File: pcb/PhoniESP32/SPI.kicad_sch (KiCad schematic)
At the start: 6 parts, among them J4 Conn_01x08_Pin

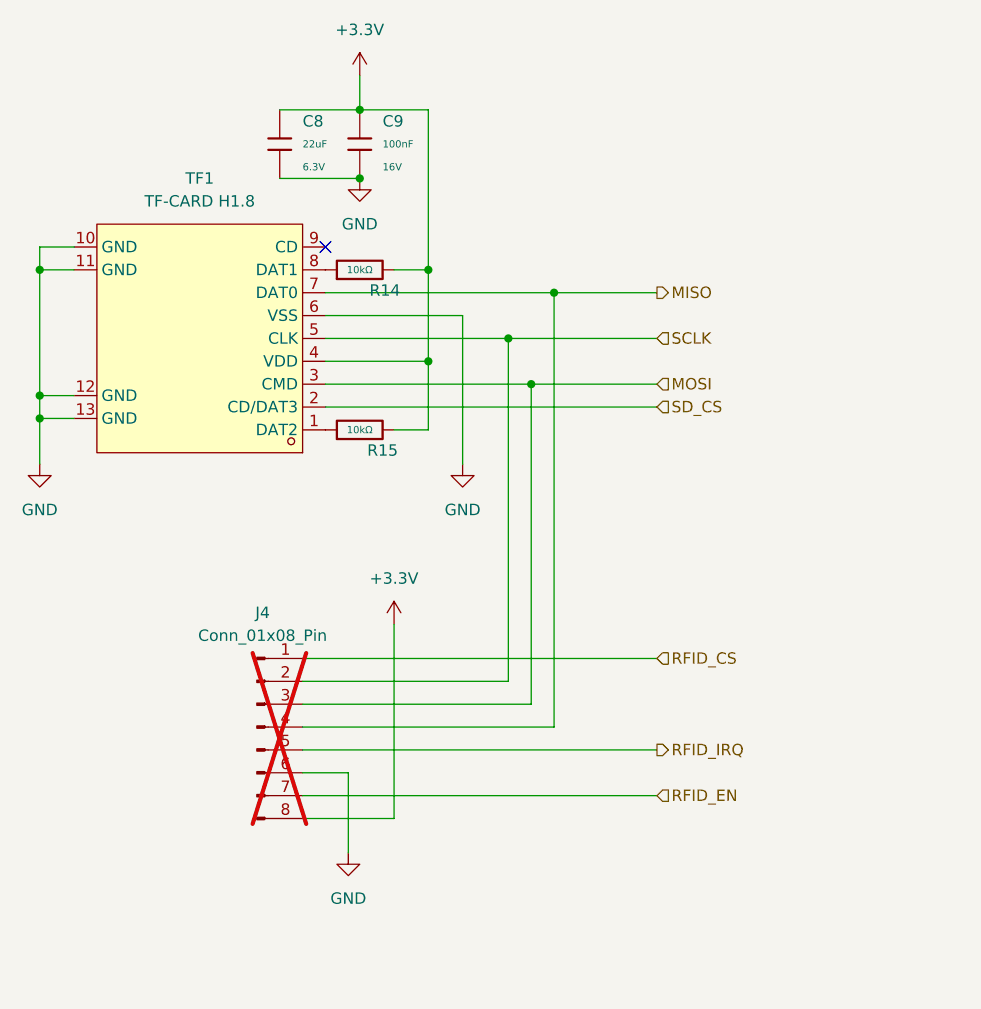
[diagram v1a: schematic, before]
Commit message: feat(pcb): version for hand soldering
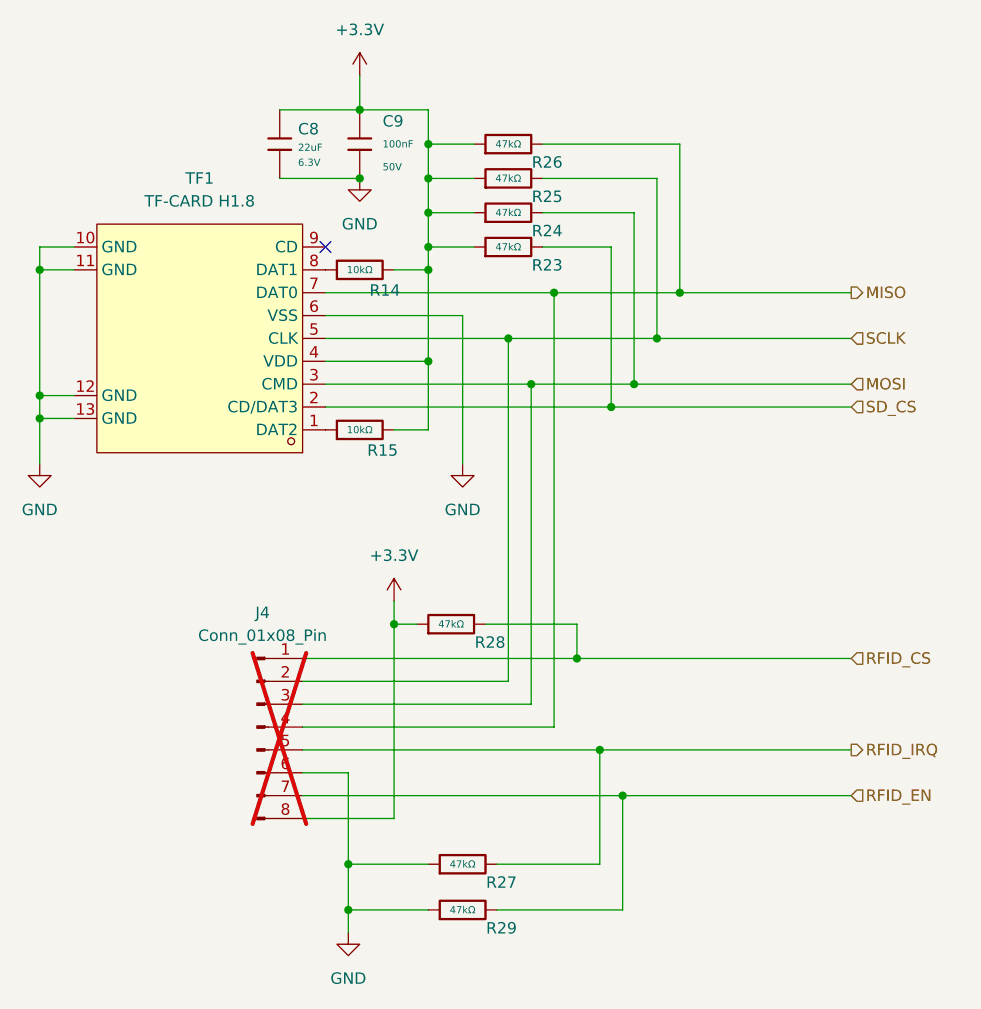
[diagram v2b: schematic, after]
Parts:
- added R23, R24, R25, R26, R27, R28, R29: 47kΩ, PCM_JLCPCB:R_0603, symbol PCM_JLCPCB-Resistors:0603,47kΩ
- C9: footprint PCM_JLCPCB:C_0402 -> PCM_JLCPCB:C_0603; symbol PCM_JLCPCB-Capacitors:0402,100nF -> PCM_JLCPCB-Capacitors:0603,100nF; LCSC C1525 -> C14663; Manufacturer Samsung Electro-Mechanics -> YAGEO; Part CL05B104KO5NNNC -> CC0603KRX7R9BB104; Price 0.004USD -> 0.006USD; Stock 20208285 -> 70324515; Voltage Rated 16V -> 50V
- J4: footprint Connector_PinSocket_2.54mm:PinSocket_1x08_P2.54mm_Vertical -> Connector_JST:JST_XH_B8B-XH-A_1x08_P2.50mm_Vertical; LCSC Part (none) -> C157972; MPN (none) -> B8B-XH-A(LF)(SN)
- TF1: MPN (none) -> TF-CARD H1.8
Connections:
- net +3.3V: now also R23.1, R24.1, R25.1, R26.1, R28.1
- net GND: now also R27.1, R29.1
- net MISO: now also R26.2
- net MOSI: now also R24.2
- net RFID_CS: now also R28.2
- net RFID_EN: now also R29.2
- net RFID_IRQ: now also R27.2
- net SCLK: now also R25.2
- net SD_CS: now also R23.2
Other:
- title: (none) -> PhoniESP32
